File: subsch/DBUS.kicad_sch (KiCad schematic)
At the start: 12 parts, among them Q1 S8050, Q6 Q_PNP_BCE, Q7 Q_PNP_BCE, U8 CH340E

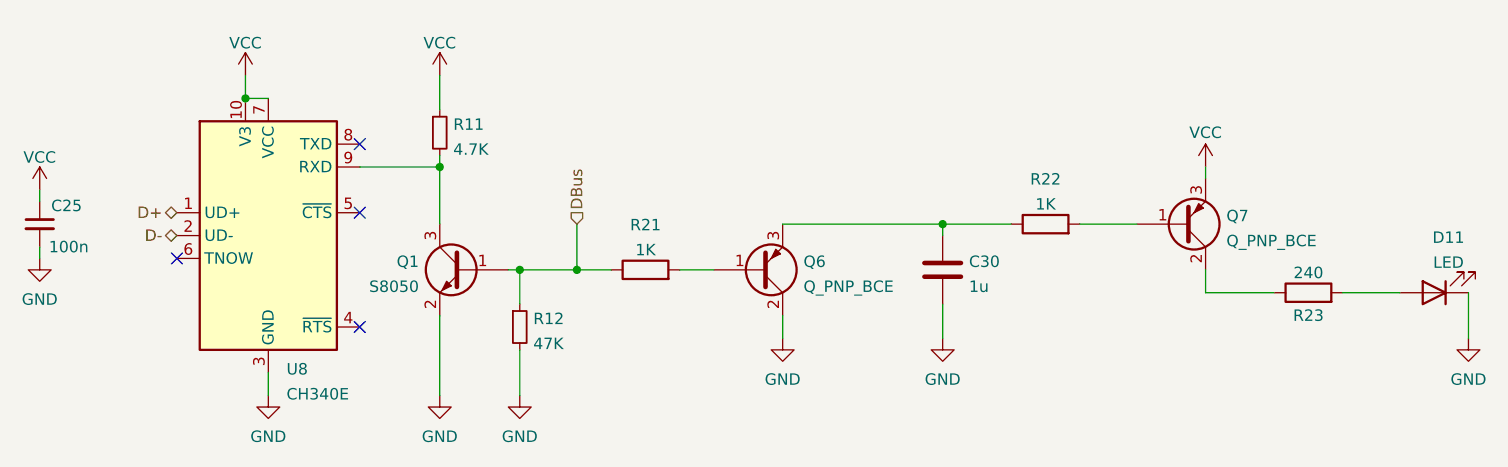
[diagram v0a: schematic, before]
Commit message: Change connectors back to GH1.25&Add ESD for UART and CAN
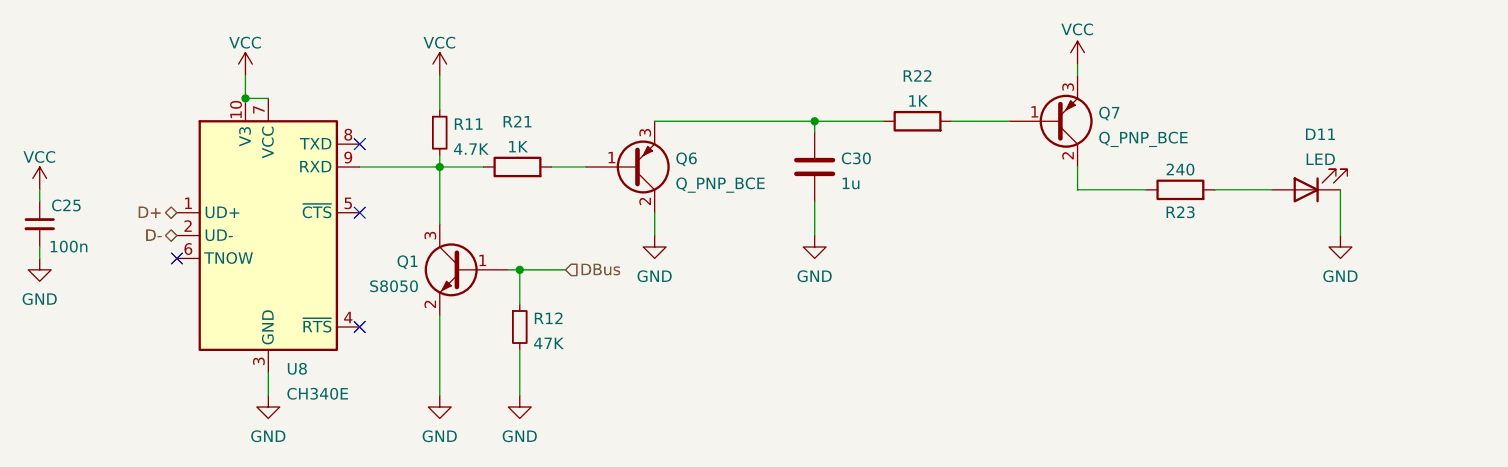
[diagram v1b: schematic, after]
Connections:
- net DBus: no longer R21.1
- net at Q1.3 (C), R11.2, U8.9 (RXD): now also R21.1
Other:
- moved on the sheet: C30, D11, Q6, Q7, R21, R22, R23

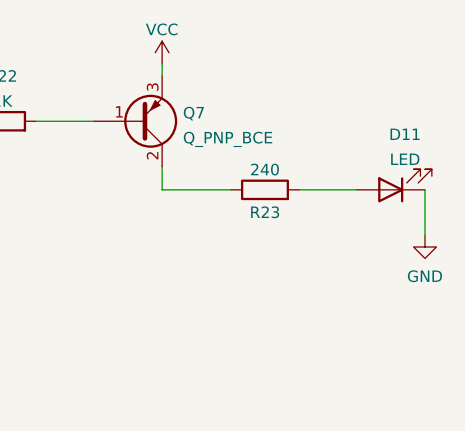
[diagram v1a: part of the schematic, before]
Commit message: Adaption for SMT
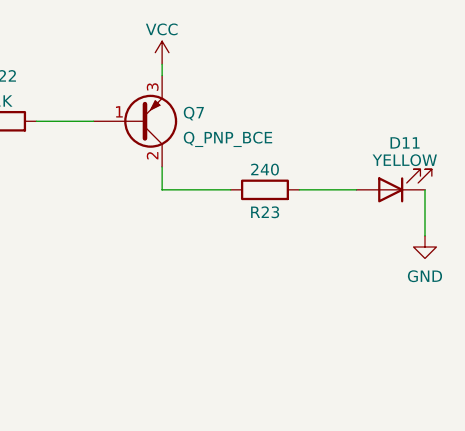
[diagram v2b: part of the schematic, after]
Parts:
- D11: value LED -> YELLOW
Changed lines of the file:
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@@
   (symbol (lib_id "Device:LED") (at 248.666 83.82 180) (unit 1)
     (in_bom yes) (on_board yes) (dnp no) (fields_autoplaced)
-    (property "Reference" "D11" (at 250.2535 77.6945 0)
+    (property "Reference" "D11" (at 250.2535 78.6511 0)
       (effects (font (size 1.27 1.27)))
     )
-    (property "Value" "LED" (at 250.2535 80.4696 0)
+    (property "Value" "YELLOW" (at 250.2535 80.5721 0)
       (effects (font (size 1.27 1.27)))
     )
